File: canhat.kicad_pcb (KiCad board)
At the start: 2 copper layers, 65 x 30 mm, 24 parts, among them J1 Raspberry_Pi_2_3, J2 CAN In, J3 CAN Out, U1 MCP2515-xSO, U2 SN65HVD234, U3 AT24C32-SSHM, Y1 16MHz

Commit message: Replaced CAN terminals with single block
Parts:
- removed J3: CAN Out, TerminalBlock_TE-Connectivity:TerminalBlock_TE_282834-2_1x02_P2.54mm_Horizontal
- J2: value CAN In -> CAN In / Out; footprint TerminalBlock_TE-Connectivity:TerminalBlock_TE_282834-2_1x02_P2.54mm_Horizontal -> TerminalBlock_TE-Connectivity:TerminalBlock_TE_282834-4_1x04_P2.54mm_Horizontal
- moved J2 6.80 mm to (44.1, 69.3)
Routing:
- net /CAN_N: track 24.0 -> 17.8 mm
- net /CAN_P: track 24.0 -> 19.0 mm
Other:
- board text added: "H OUT L IN H"
- board text added: "Raspberry Pi CAN HAT © 2019 onitake V2"
- board text removed: "H"
- board text removed: "IN"
- board text removed: "L"
- board text removed: "OUT"
- board text removed: "Raspberry Pi CAN HAT © 2019 onitake V1"

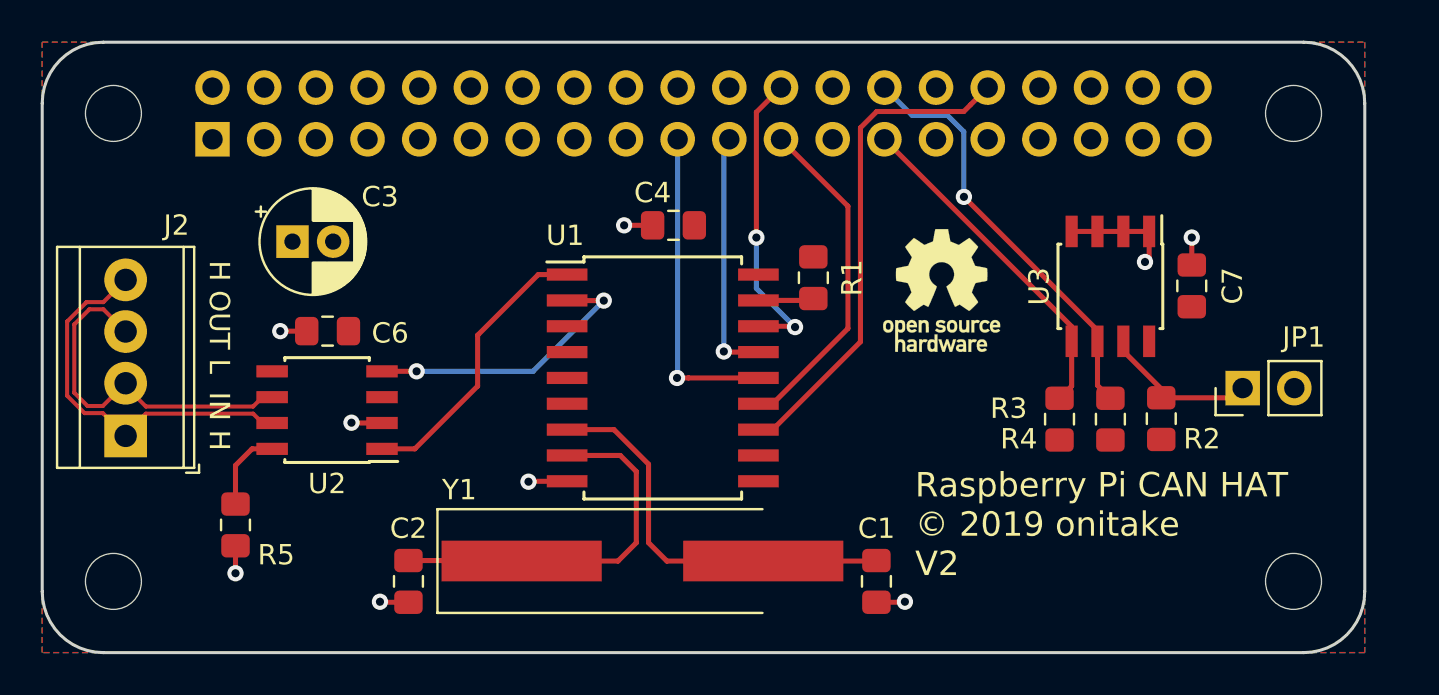
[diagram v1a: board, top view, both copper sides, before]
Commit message: Added 5V power terminal
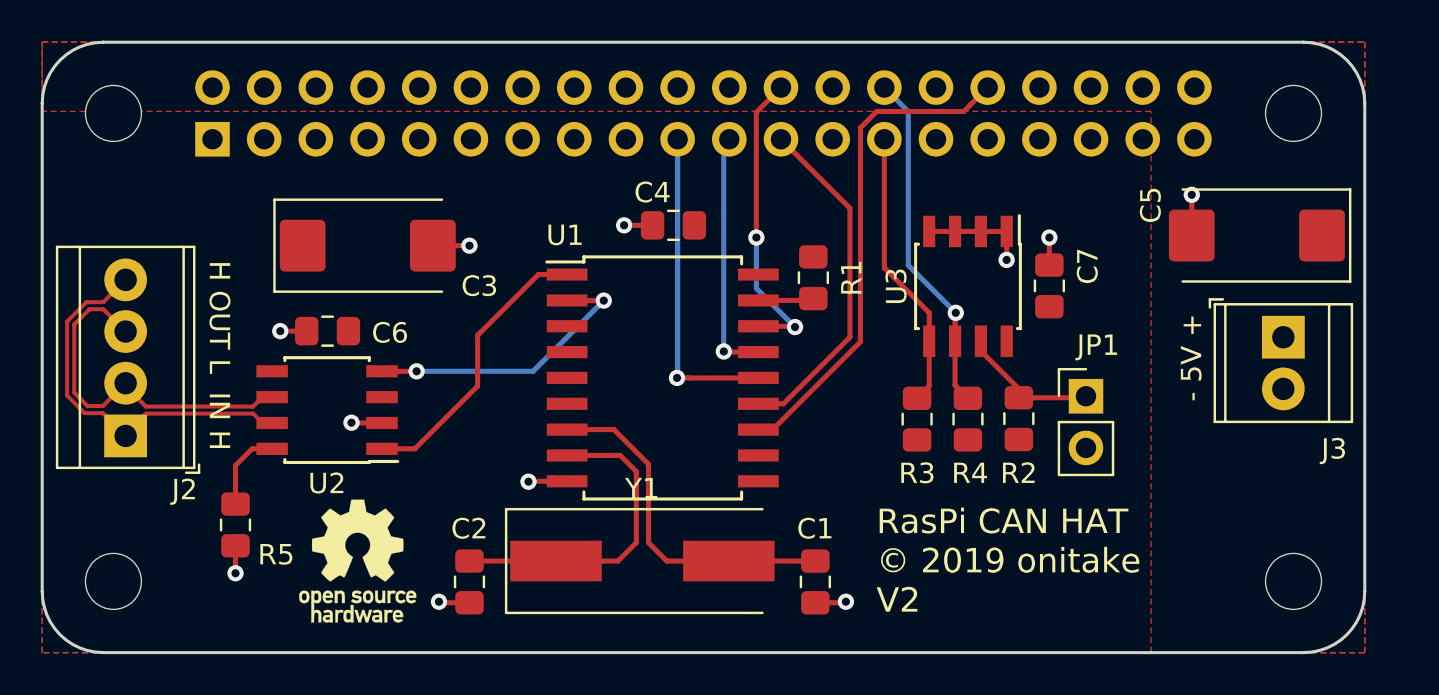
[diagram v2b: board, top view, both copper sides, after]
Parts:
- added C5: 10u, Capacitor_Tantalum_SMD:CP_EIA-7343-31_Kemet-D_Pad2.25x2.55mm_HandSolder, F.Cu at (99.7, 59.5)
- added J3: 5V, TerminalBlock_TE-Connectivity:TerminalBlock_TE_282834-2_1x02_P2.54mm_Horizontal, F.Cu at (101.0, 64.5)
- C3: footprint Capacitor_THT:CP_Radial_D5.0mm_P2.00mm -> Capacitor_Tantalum_SMD:CP_EIA-7343-31_Kemet-D_Pad2.25x2.55mm_HandSolder
- Y1: footprint Crystal:Crystal_SMD_HC49-SD_HandSoldering -> Crystal:Crystal_SMD_HC49-SD
- moved OSHW1 31.6 mm to (55.5, 75.5)
- moved JP1 7.71 mm to (91.3, 67.4), turned to 0 degrees
- moved C7 7.00 mm to (89.5, 62.0)
- moved R2 7.00 mm to (88.0, 68.5)
- moved R3 7.00 mm to (83.0, 68.5)
- moved R4 7.00 mm to (85.5, 68.5)
- moved U3 7.00 mm to (85.5, 62.0)
- moved C3 3.71 mm to (56.0, 60.0)
- moved C1 3.00 mm to (78.0, 76.5)
- moved C2 3.00 mm to (61.0, 76.5)
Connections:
- J1 pad 2: (no net) -> +5V
- J1 pad 4: (no net) -> +5V
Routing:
- net /ID_SC: track 20.9 -> 17.0 mm
- net GND: track 17.0 -> 20.9 mm, vias 9 -> 11
- net /ID_SD: track 16.8 -> 13.9 mm
- net Net-(C2-Pad2): track 18.8 -> 17.5 mm
- net Net-(C1-Pad1): track 20.1 -> 18.8 mm
- added copper zone on F.Cu, net +5V
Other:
- board text added: "- 5V +"
- board text added: "RasPi CAN HAT © 2019 onitake V2"
- board text removed: "Raspberry Pi CAN HAT © 2019 onitake V2"

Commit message: Optimized traces
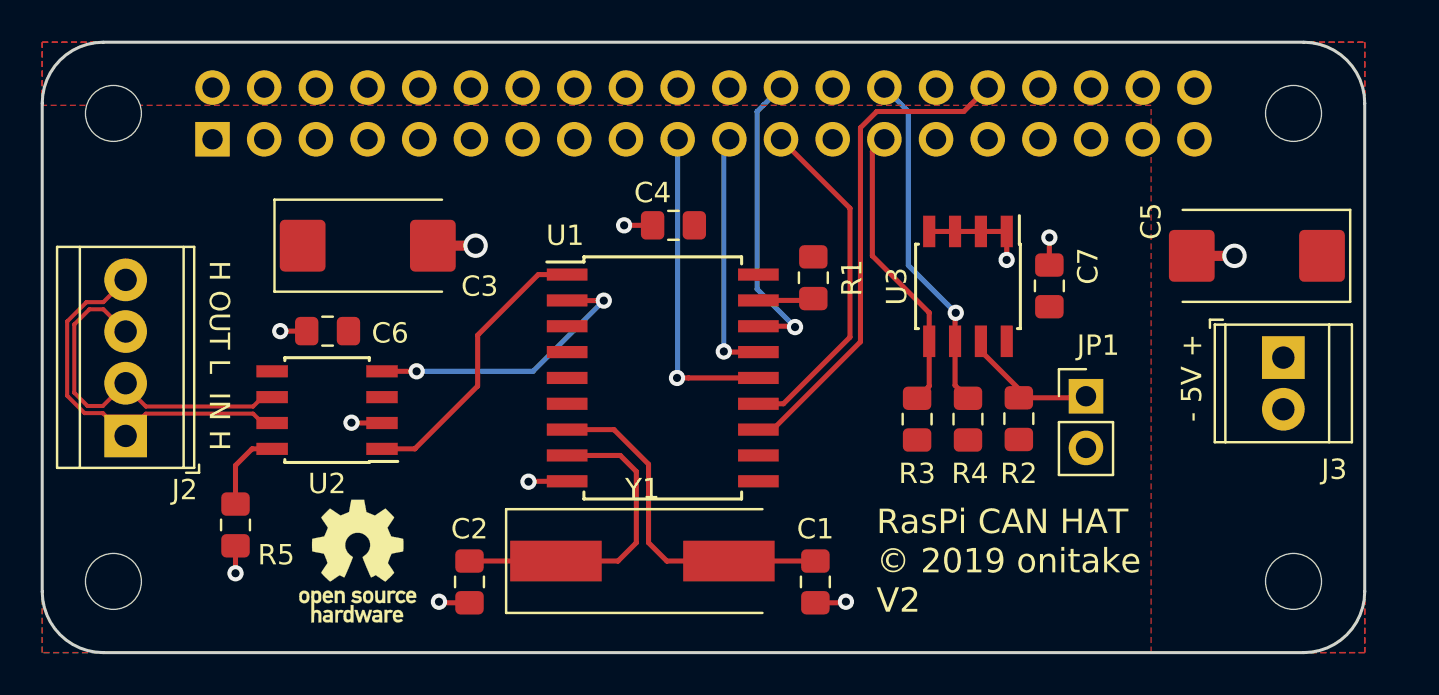
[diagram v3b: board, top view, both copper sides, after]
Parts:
- moved C5 1.00 mm to (99.7, 60.5)
- moved J3 1.00 mm to (101.0, 65.5)
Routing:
- net /~CS: track 14.9 -> 14.8 mm, vias 2 -> 1
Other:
- net class Power added: clearance 0.2, trace_width 0.5, via_dia 1.2, via_drill 0.8
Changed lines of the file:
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@@
   )
   (setup
-    (last_trace_width 0.25)
+    (last_trace_width 0.5)
+    (user_trace_width 0.5)
     (trace_clearance 0.2)
     (zone_clearance 0.25)
@@
     (via_min_size 0.4)
     (via_min_drill 0.3)
+    (user_via 1.2 0.8)
     (uvia_size 0.3)
     (uvia_drill 0.1)
@@
     (solder_mask_min_width 0.25)
     (aux_axis_origin 40 50)
-    (grid_origin 40 50)
     (visible_elements FFFFFF7F)
     (pcbplotparams
@@
     (add_net /CAN_N)
     (add_net /CAN_P)
+  )
+  (net_class Power ""
+    (clearance 0.2)
+    (trace_width 0.5)
+    (via_dia 1.2)
+    (via_drill 0.8)
+    (uvia_dia 0.3)
+    (uvia_drill 0.1)
   )
   (module TerminalBlock_TE-Connectivity:TerminalBlock_TE_282834-4_1x04_P2.54mm_Horizontal (layer F.Cu)
@@
   )
   (module Capacitor_Tantalum_SMD:CP_EIA-7343-31_Kemet-D_Pad2.25x2.55mm_HandSolder (layer F.Cu)
-    (at 99.7 59.5 180)
+    (at 99.7 60.5 180)
     (descr "Tantalum Capacitor SMD Kemet-D (7343-31 Metric), IPC_7351 nominal, (Body size from: http://www.kemet.com/Lists/ProductCatalog/Attachments/253/KEM_TC101_STD.pdf), generated with kicad-footprint-generator")
     (tags "capacitor tantalum")
     (attr smd)
-    (fp_text reference C5 (at 5.2 1.5 270) (layer F.SilkS)
+    (fp_text reference C5 (at 5.2 1.7 270) (layer F.SilkS)
       (effects (font (size 1 1) (thickness 0.15)))
     )
@@
   )
   (module TerminalBlock_TE-Connectivity:TerminalBlock_TE_282834-2_1x02_P2.54mm_Horizontal (layer F.Cu)
-    (at 101 64.5 270)
+    (at 101 65.5 270)
     (descr "Terminal Block TE 282834-2, 2 pins, pitch 2.54mm, size 5.54x6.5mm^2, drill diamater 1.1mm, pad diameter 2.1mm, see http://www.te.com/commerce/DocumentDelivery/DDEController?Action=showdoc&DocId=Customer+Drawing%7F282834%7FC1%7Fpdf%7FEnglish%7FENG_CD_282834_C1.pdf, script-generated using https://github.com/pointhi/kicad-footprint-generator/scripts/TerminalBlock_TE-Connectivity")
     (tags "THT Terminal Block TE 282834-2 pitch 2.54mm size 5.54x6.5mm^2 drill 1.1mm pad 2.1mm")
@@
     )
   )
-  (gr_text "- 5V +" (at 96.5 65.5 90) (layer F.SilkS)
+  (gr_text "- 5V +" (at 96.5 66.5 90) (layer F.SilkS)
     (effects (font (size 1 1) (thickness 0.15)))
   )
@@
   (segment (start 87.405 59.3) (end 87.405 60.695) (width 0.25) (layer F.Cu) (net 3))
   (segment (start 87.405 60.695) (end 87.4 60.7) (width 0.25) (layer F.Cu) (net 3))
-  (via (at 96.5 57.5) (size 0.8) (drill 0.4) (layers F.Cu B.Cu) (net 3))
-  (segment (start 96.5 59.5) (end 96.5 57.5) (width 0.25) (layer F.Cu) (net 3))
-  (segment (start 59.2 60) (end 61 60) (width 0.25) (layer F.Cu) (net 3) (status 1000000))
-  (via (at 61 60) (size 0.8) (drill 0.4) (layers F.Cu B.Cu) (net 3) (status 1000000))
-  (segment (start 85.620001 53.079999) (end 86.47 52.23) (width 0.25) (layer F.Cu) (net 4) (status 30))
+  (via (at 61.3 60) (size 1.2) (drill 0.8) (layers F.Cu B.Cu) (net 3))
+  (segment (start 59.2 60) (end 61.3 60) (width 0.5) (layer F.Cu) (net 3))
+  (via (at 98.6 60.5) (size 1.2) (drill 0.8) (layers F.Cu B.Cu) (net 3))
+  (segment (start 96.5 60.5) (end 98.6 60.5) (width 0.5) (layer F.Cu) (net 3))
   (segment (start 85.294999 53.405001) (end 85.620001 53.079999) (width 0.25) (layer F.Cu) (net 4) (status 20))
   (segment (start 80.214999 54.205999) (end 81.015997 53.405001) (width 0.25) (layer F.Cu) (net 4))
+  (segment (start 80.214999 64.725001) (end 80.214999 54.205999) (width 0.25) (layer F.Cu) (net 4))
   (segment (start 81.015997 53.405001) (end 85.294999 53.405001) (width 0.25) (layer F.Cu) (net 4))
   (segment (start 75.9 69.04) (end 80.214999 64.725001) (width 0.25) (layer F.Cu) (net 4) (status 10))
-  (segment (start 80.214999 64.725001) (end 80.214999 54.205999) (width 0.25) (layer F.Cu) (net 4))
   (segment (start 75.2 69.04) (end 75.9 69.04) (width 0.25) (layer F.Cu) (net 4) (status 30))
-  (segment (start 75.2 67.77) (end 76.43 67.77) (width 0.25) (layer F.Cu) (net 5))
-  (segment (start 76.43 67.77) (end 79.7 64.5) (width 0.25) (layer F.Cu) (net 5))
-  (segment (start 79.7 58.16) (end 76.31 54.77) (width 0.25) (layer F.Cu) (net 5))
-  (segment (start 79.7 64.5) (end 79.7 58.16) (width 0.25) (layer F.Cu) (net 5))
+  (segment (start 85.620001 53.079999) (end 86.47 52.23) (width 0.25) (layer F.Cu) (net 4) (status 30))
+  (segment (start 76.43 67.77) (end 75.2 67.77) (width 0.25) (layer F.Cu) (net 5))
+  (segment (start 79.7 64.5) (end 76.43 67.77) (width 0.25) (layer F.Cu) (net 5))
+  (segment (start 79.7 58.16) (end 79.7 64.5) (width 0.25) (layer F.Cu) (net 5))
+  (segment (start 76.31 54.77) (end 79.7 58.16) (width 0.25) (layer F.Cu) (net 5))
   (via (at 71.2 66.5) (size 0.8) (drill 0.4) (layers F.Cu B.Cu) (net 6))
   (segment (start 71.23 54.77) (end 71.23 66.47) (width 0.25) (layer B.Cu) (net 6))
@@
   (via (at 77 64) (size 0.8) (drill 0.4) (layers F.Cu B.Cu) (net 8))
   (segment (start 76.96 63.96) (end 77 64) (width 0.25) (layer F.Cu) (net 8))
-  (via (at 75.1 59.6) (size 0.8) (drill 0.4) (layers F.Cu B.Cu) (net 8))
-  (segment (start 77 64) (end 75.1 62.1) (width 0.25) (layer B.Cu) (net 8))
-  (segment (start 75.1 62.1) (end 75.1 59.6) (width 0.25) (layer B.Cu) (net 8))
-  (segment (start 75.1 53.44) (end 76.31 52.23) (width 0.25) (layer F.Cu) (net 8) (status 20))
-  (segment (start 75.1 59.6) (end 75.1 53.44) (width 0.25) (layer F.Cu) (net 8))
+  (segment (start 75.134999 53.405001) (end 75.460001 53.079999) (width 0.25) (layer B.Cu) (net 8))
+  (segment (start 75.460001 53.079999) (end 76.31 52.23) (width 0.25) (layer B.Cu) (net 8))
+  (segment (start 75.134999 62.134999) (end 75.134999 53.405001) (width 0.25) (layer B.Cu) (net 8))
+  (segment (start 77 64) (end 75.134999 62.134999) (width 0.25) (layer B.Cu) (net 8))
   (segment (start 78.01 62.69) (end 78.1 62.6) (width 0.25) (layer F.Cu) (net 9) (status 30))
   (segment (start 77.81 62.69) (end 77.9 62.6) (width 0.25) (layer F.Cu) (net 9) (status 30))
@@
   (segment (start 83.595 64.7) (end 83.595 66.905) (width 0.25) (layer F.Cu) (net 11) (status 10))
   (segment (start 83.595 63.295) (end 83.595 64.7) (width 0.25) (layer F.Cu) (net 11))
-  (segment (start 81.39 61.09) (end 83.595 63.295) (width 0.25) (layer F.Cu) (net 11))
-  (segment (start 81.39 54.77) (end 81.39 61.09) (width 0.25) (layer F.Cu) (net 11))
+  (segment (start 80.8 60.5) (end 83.595 63.295) (width 0.25) (layer F.Cu) (net 11))
+  (segment (start 80.8 55.36) (end 80.8 60.5) (width 0.25) (layer F.Cu) (net 11))
+  (segment (start 81.39 54.77) (end 80.8 55.36) (width 0.25) (layer F.Cu) (net 11))
   (segment (start 84.865 66.865) (end 85.5 67.5) (width 0.25) (layer F.Cu) (net 12) (status 20))
   (segment (start 84.865 64.7) (end 84.865 66.865) (width 0.25) (layer F.Cu) (net 12) (status 10))
@@
     (polygon
       (pts
-        (xy 40 50) (xy 105 50) (xy 105 80) (xy 94.5 80) (xy 94.5 58.7)
-        (xy 94.5 53.4) (xy 40 53.4)
+        (xy 40 50) (xy 105 50) (xy 105 80) (xy 94.5 80) (xy 94.5 53.1)
+        (xy 40 53.1)
       )
     )

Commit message: Small track optimisations
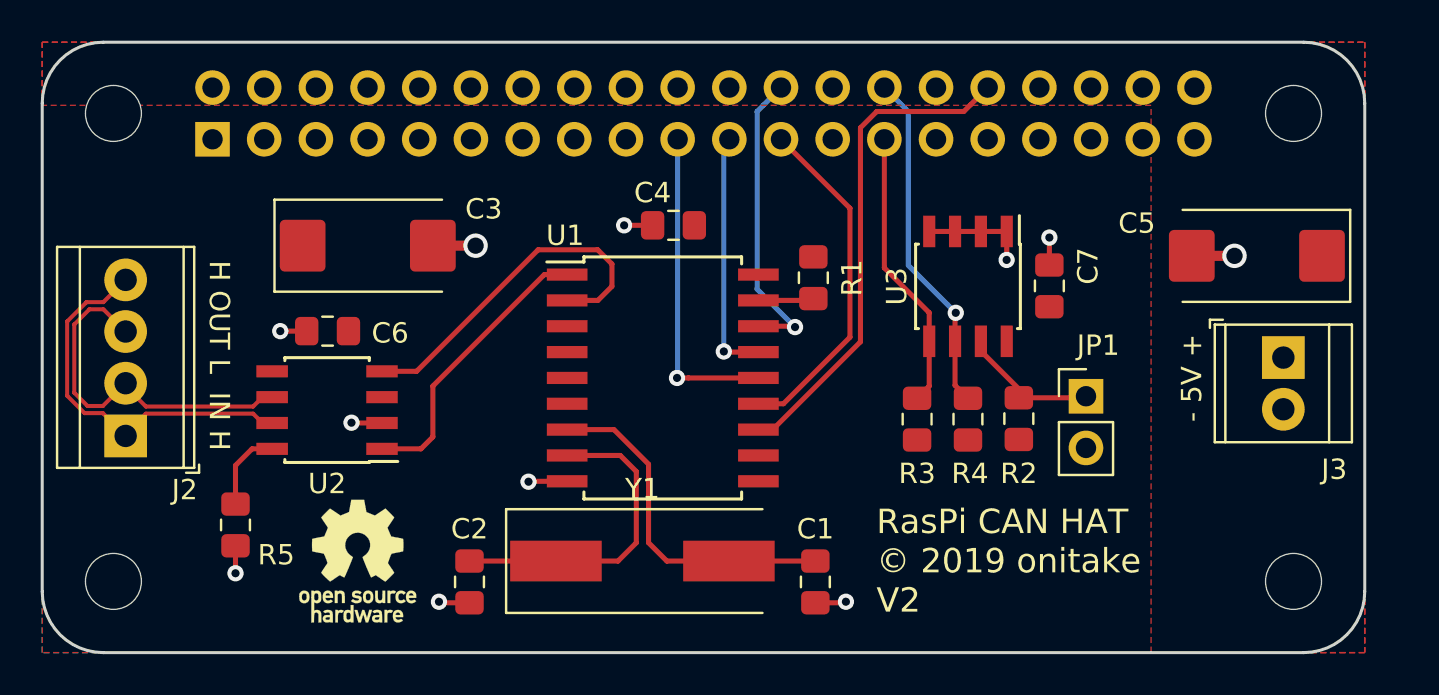
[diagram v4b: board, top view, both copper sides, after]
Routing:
- net /RX: track 14.1 -> 17.7 mm, vias 2 -> 0
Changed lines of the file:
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@@
     (thickness 1.6)
     (drawings 13)
-    (tracks 131)
+    (tracks 129)
     (zones 0)
     (modules 25)
@@
   (title_block
     (title "CAN HAT for Raspberry Pi")
-    (date 2019-05-01)
+    (date 2019-05-02)
     (rev 2)
-    (company "Gregor Riepl <onitake@gmail.com>")
+    (company "© 2019 Gregor Riepl")
   )
   (layers
@@
   )
   (setup
-    (last_trace_width 0.5)
+    (last_trace_width 0.25)
     (user_trace_width 0.5)
     (trace_clearance 0.2)
@@
     (tags "capacitor tantalum")
     (attr smd)
-    (fp_text reference C5 (at 5.2 1.7 270) (layer F.SilkS)
+    (fp_text reference C5 (at 5.9 1.6) (layer F.SilkS)
       (effects (font (size 1 1) (thickness 0.15)))
     )
@@
     (tags "capacitor tantalum")
     (attr smd)
-    (fp_text reference C3 (at 5.5 2) (layer F.SilkS)
+    (fp_text reference C3 (at 5.7 -1.8) (layer F.SilkS)
       (effects (font (size 1 1) (thickness 0.15)))
     )
@@
   (segment (start 83.595 64.7) (end 83.595 66.905) (width 0.25) (layer F.Cu) (net 11) (status 10))
   (segment (start 83.595 63.295) (end 83.595 64.7) (width 0.25) (layer F.Cu) (net 11))
-  (segment (start 80.8 60.5) (end 83.595 63.295) (width 0.25) (layer F.Cu) (net 11))
-  (segment (start 80.8 55.36) (end 80.8 60.5) (width 0.25) (layer F.Cu) (net 11))
-  (segment (start 81.39 54.77) (end 80.8 55.36) (width 0.25) (layer F.Cu) (net 11))
+  (segment (start 81.39 61.09) (end 83.595 63.295) (width 0.25) (layer F.Cu) (net 11))
+  (segment (start 81.39 54.77) (end 81.39 61.09) (width 0.25) (layer F.Cu) (net 11))
   (segment (start 84.865 66.865) (end 85.5 67.5) (width 0.25) (layer F.Cu) (net 12) (status 20))
   (segment (start 84.865 64.7) (end 84.865 66.865) (width 0.25) (layer F.Cu) (net 12) (status 10))
@@
   (segment (start 91.525 67.475) (end 92 67) (width 0.25) (layer F.Cu) (net 13) (status 30))
   (segment (start 88 67.475) (end 91.525 67.475) (width 0.25) (layer F.Cu) (net 13) (status 30))
-  (segment (start 61.4 64.4) (end 61.4 66.9) (width 0.25) (layer F.Cu) (net 14))
-  (segment (start 58.315 69.985) (end 56.7 69.985) (width 0.25) (layer F.Cu) (net 14))
-  (segment (start 61.4 66.9) (end 58.315 69.985) (width 0.25) (layer F.Cu) (net 14))
-  (segment (start 65.8 61.42) (end 64.38 61.42) (width 0.25) (layer F.Cu) (net 14))
-  (segment (start 64.38 61.42) (end 61.4 64.4) (width 0.25) (layer F.Cu) (net 14))
-  (via (at 67.6 62.7) (size 0.8) (drill 0.4) (layers F.Cu B.Cu) (net 15))
-  (segment (start 65.81 62.7) (end 65.8 62.69) (width 0.25) (layer F.Cu) (net 15))
-  (segment (start 67.6 62.7) (end 65.81 62.7) (width 0.25) (layer F.Cu) (net 15))
-  (via (at 58.4 66.175) (size 0.8) (drill 0.4) (layers F.Cu B.Cu) (net 15))
+  (segment (start 56.7 69.985) (end 58.615 69.985) (width 0.25) (layer F.Cu) (net 14))
+  (segment (start 58.615 69.985) (end 59.2 69.4) (width 0.25) (layer F.Cu) (net 14))
+  (segment (start 64.68 61.42) (end 59.2 66.9) (width 0.25) (layer F.Cu) (net 14))
+  (segment (start 65.8 61.42) (end 64.68 61.42) (width 0.25) (layer F.Cu) (net 14))
+  (segment (start 59.2 69.4) (end 59.2 66.9) (width 0.25) (layer F.Cu) (net 14))
+  (segment (start 67.31 62.69) (end 65.8 62.69) (width 0.25) (layer F.Cu) (net 15))
+  (segment (start 58.4 66.175) (end 64.375 60.2) (width 0.25) (layer F.Cu) (net 15))
   (segment (start 56.7 66.175) (end 58.4 66.175) (width 0.25) (layer F.Cu) (net 15))
-  (segment (start 58.70336 66.175) (end 58.4 66.175) (width 0.25) (layer B.Cu) (net 15))
-  (segment (start 67.6 62.7) (end 64.125 66.175) (width 0.25) (layer B.Cu) (net 15))
-  (segment (start 64.125 66.175) (end 58.70336 66.175) (width 0.25) (layer B.Cu) (net 15))
+  (segment (start 67.3 60.2) (end 68 60.9) (width 0.25) (layer F.Cu) (net 15))
+  (segment (start 64.375 60.2) (end 67.3 60.2) (width 0.25) (layer F.Cu) (net 15))
+  (segment (start 68 60.9) (end 68 62) (width 0.25) (layer F.Cu) (net 15))
+  (segment (start 68 62) (end 67.31 62.69) (width 0.25) (layer F.Cu) (net 15))
   (segment (start 45.095 68.255) (end 44 69.35) (width 0.2) (layer F.Cu) (net 16))
   (segment (start 50.365 68.255) (end 45.095 68.255) (width 0.2) (layer F.Cu) (net 16))
